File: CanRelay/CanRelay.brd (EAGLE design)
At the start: 93 x 65.5 mm, 24 parts

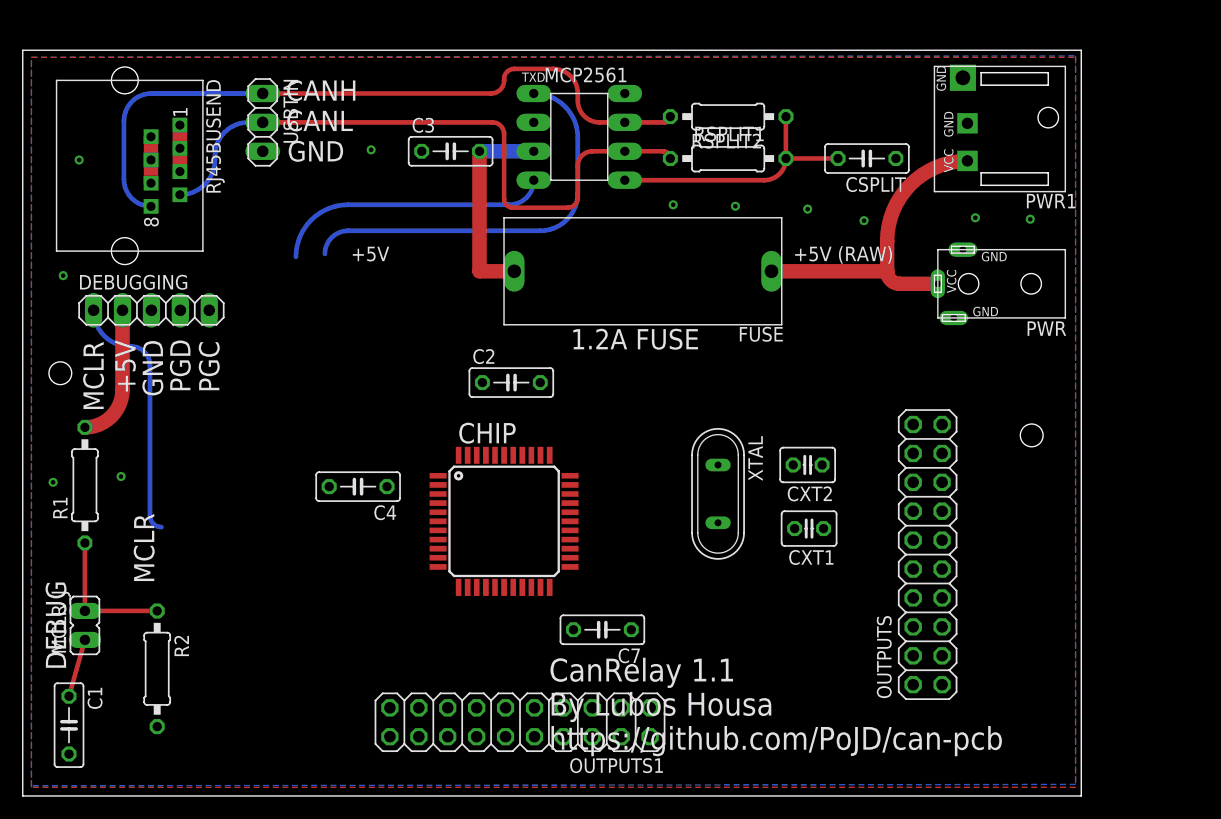
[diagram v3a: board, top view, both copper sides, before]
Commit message: #19 connected all but output ports, including RXD and TXD on both schema and the board, with no erc errors. Rotated the chip in the end to get MCLR and programming up and RX and TX closer to the transceiver. all seems sort of OKish so far, missing all outputs which are likely to mess things up
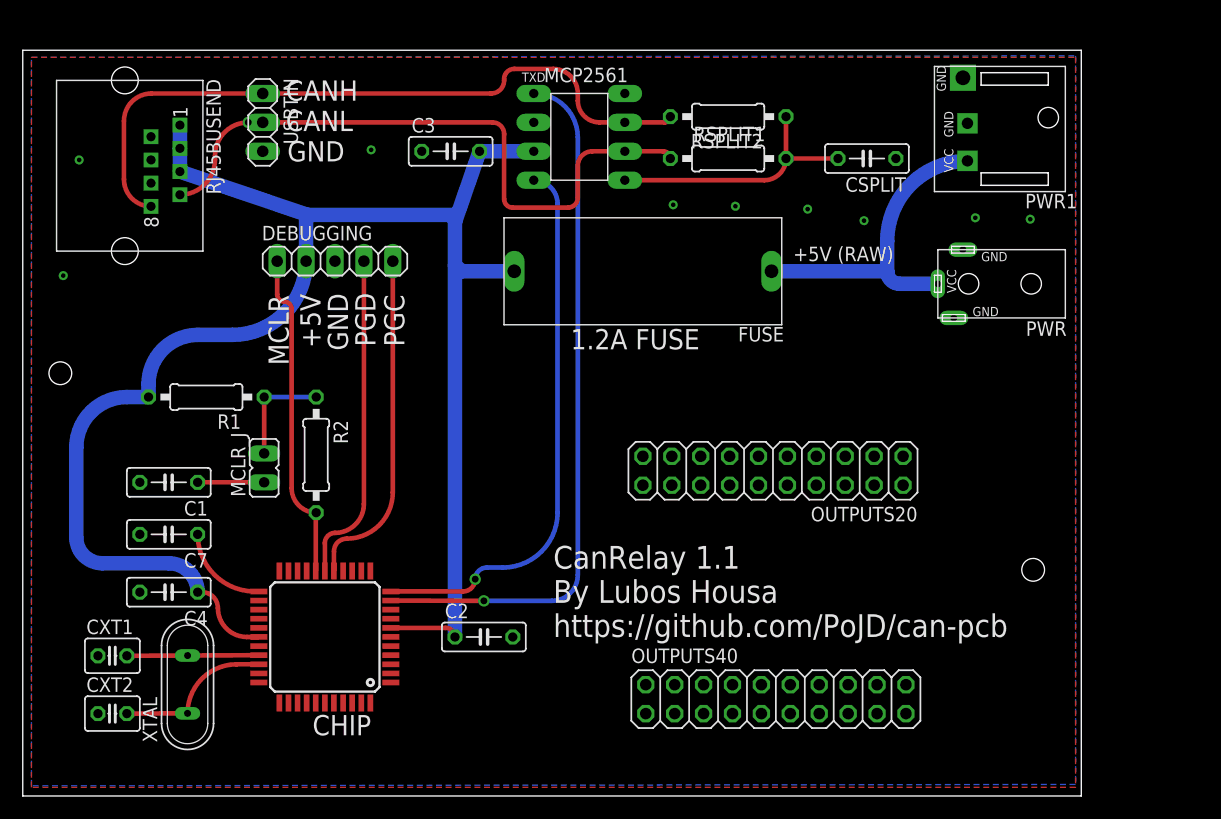
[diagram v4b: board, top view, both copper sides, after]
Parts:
- removed OUTPUTS, OUTPUTS1: (no value), pinhead:2X10
- added OUTPUTS20, OUTPUTS40: (no value), pinhead:2X10
- moved CXT2 64.9 mm to (7.87, 7.24), turned to 0 degrees
- moved CXT1 62.2 mm to (7.87, 12.3), turned to 0 degrees
- moved XTAL 49.5 mm to (14.5, 9.80), turned to 90 degrees
- moved C7 39.0 mm to (12.8, 23.0)
- moved R2 23.4 mm to (25.8, 30.0)
- moved C1 23.1 mm to (12.8, 27.6), turned to 180 degrees
- moved C2 22.5 mm to (40.5, 14.0)
- moved MCLR_J 21.0 mm to (21.2, 28.8)
- moved C4 19.0 mm to (12.8, 17.9)
- moved CHIP 18.7 mm to (26.5, 14.0), turned to 180 degrees
- moved DEBUGGING 16.7 mm to (27.4, 47.0)
- moved R1 13.2 mm to (16.1, 35.1), turned to 180 degrees
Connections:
- removed net N$4: C7.2, CHIP.23
- removed net PGC/O15: DEBUGGING.5, OUTPUTS.18
- removed net PGD/O16: DEBUGGING.4, OUTPUTS.20
- new net ENVREG: C7.1, CHIP.23
- new net O15: OUTPUTS20.18
- new net O16: OUTPUTS20.20
- new net PGC: CHIP.16, DEBUGGING.5
- new net PGD: CHIP.17, DEBUGGING.4
- net GND: now also C7.2; no longer C7.1
- net O1: now also OUTPUTS20.17; no longer OUTPUTS.17
- net O10: now also OUTPUTS20.12; no longer OUTPUTS.12
- net O13: now also OUTPUTS20.14; no longer OUTPUTS.14
- net O14: now also OUTPUTS20.16; no longer OUTPUTS.16
- net O17: now also OUTPUTS20.7; no longer OUTPUTS.7
- net O18: now also OUTPUTS20.5; no longer OUTPUTS.5
- net O19: now also OUTPUTS20.3; no longer OUTPUTS.3
- net O2: now also OUTPUTS20.15; no longer OUTPUTS.15
- net O20: now also OUTPUTS20.1; no longer OUTPUTS.1
- net O21: now also OUTPUTS20.2; no longer OUTPUTS.2
- net O22: now also OUTPUTS20.4; no longer OUTPUTS.4
- net O23: now also OUTPUTS20.6; no longer OUTPUTS.6
- net O24: now also OUTPUTS20.8; no longer OUTPUTS.8
- net O3: now also OUTPUTS20.13; no longer OUTPUTS.13
- net O4: now also OUTPUTS20.11; no longer OUTPUTS.11
- net O6: now also OUTPUTS20.9; no longer OUTPUTS.9
- net O9: now also OUTPUTS20.10; no longer OUTPUTS.10
- net RXD: now also CHIP.11
- net TXD: now also CHIP.10
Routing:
- net +5V: track 35.0 -> 148.0 mm
- net PGC: track 0.00 -> 29.4 mm
- net PGD: track 0.00 -> 28.6 mm
- net TXD: track 34.8 -> 61.3 mm, vias 0 -> 1
- net RXD: track 23.7 -> 47.6 mm, vias 0 -> 1
- net OSC2: track 0.00 -> 13.4 mm
- net OSC1: track 0.00 -> 11.6 mm
- net ENVREG: track 0.00 -> 7.45 mm
- net MCLR: track 21.6 -> 28.7 mm
- net GND: track 4.08 -> 0.00 mm, vias 11 -> 9
- net N$2: track 12.3 -> 9.52 mm
- net N$1: track 5.15 -> 5.84 mm
- net CANL: vias 0 -> 1
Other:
- board text removed: "DEBUG"
- board text removed: "RXD"
- board text removed: "TXD"

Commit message: #19 started connecting output ports. Bottom pat all done, also labeled properly, moved the whole PCB a few mms up to make space for routes there
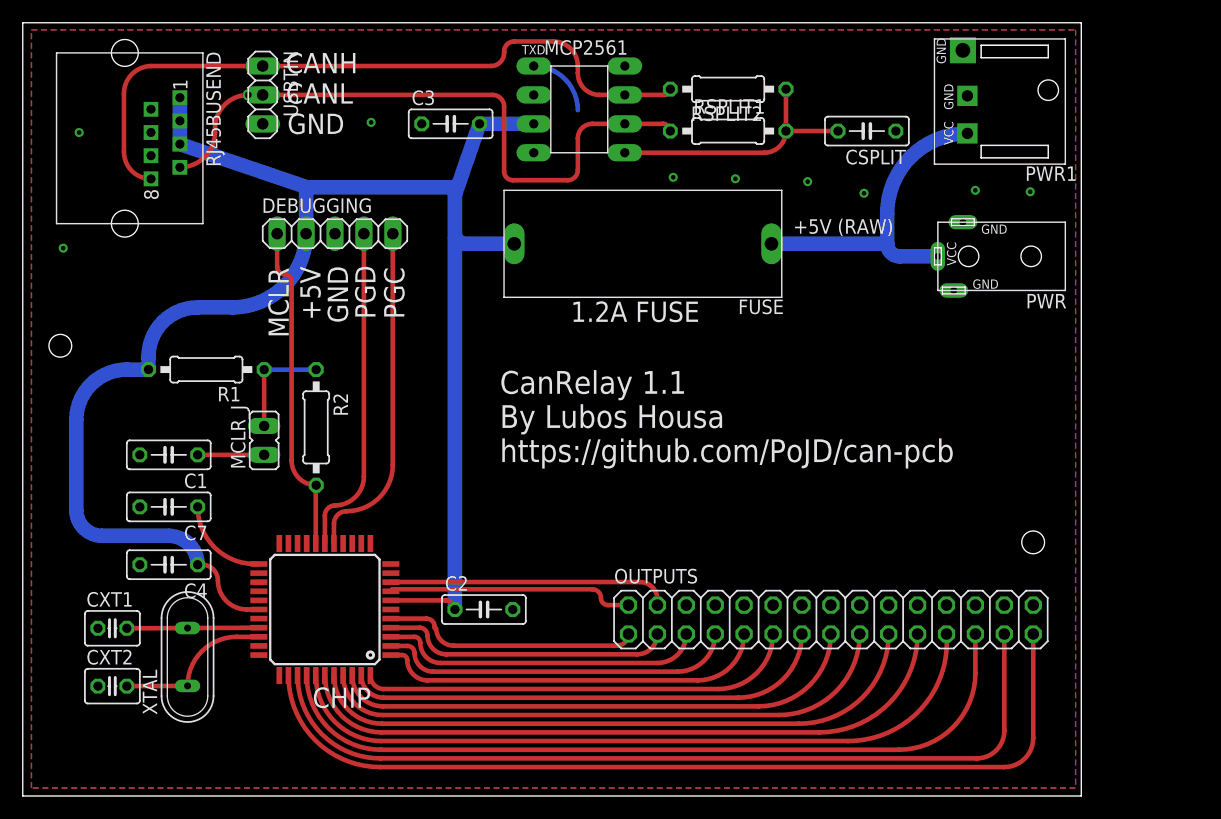
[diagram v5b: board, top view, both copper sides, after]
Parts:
- removed OUTPUTS20, OUTPUTS40: (no value), pinhead:2X10
- added OUTPUTS: (no value), pinhead:2X15
- moved CSPLIT 2.41 mm to (74.2, 58.4)
- moved FUSE 2.41 mm to (54.5, 48.5)
- moved MCP2561 2.41 mm to (48.9, 60.3)
- moved R1 2.41 mm to (16.1, 37.5)
- moved RSPLIT1 2.41 mm to (62.0, 58.4)
- moved RSPLIT2 2.41 mm to (62.0, 62.1)
- moved C1 2.41 mm to (12.8, 30.0)
- moved C4 2.41 mm to (12.8, 20.3)
- moved C7 2.41 mm to (12.8, 25.4)
- moved MCLR_J 2.41 mm to (21.2, 31.2)
- moved CXT2 2.41 mm to (7.87, 9.65)
- moved C2 2.41 mm to (40.5, 16.4)
- moved CHIP 2.41 mm to (26.5, 16.4)
- moved CXT1 2.41 mm to (7.87, 14.7)
- moved XTAL 2.41 mm to (14.5, 12.2)
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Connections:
- new net N$10: CHIP.14
- new net N$11: CHIP.15
- new net N$12: CHIP.19
- new net N$13: CHIP.20
- new net N$14: CHIP.21
- new net N$15: CHIP.22
- new net N$25: CHIP.27
- new net N$26: CHIP.26
- new net N$27: CHIP.25
- new net N$28: CHIP.24
- new net O11: CHIP.44, OUTPUTS.11
- new net O12: OUTPUTS.12
- new net O25: CHIP.37, OUTPUTS.25
- new net O26: OUTPUTS.26
- new net O27: CHIP.36, OUTPUTS.27
- new net O28: OUTPUTS.28
- new net O29: CHIP.35, OUTPUTS.29
- new net O30: CHIP.32, OUTPUTS.30
- new net O5: CHIP.3, OUTPUTS.5
- new net O7: CHIP.2, OUTPUTS.7
- new net O8: OUTPUTS.8
- net O1: now also CHIP.5, OUTPUTS.1; no longer OUTPUTS20.17
- net O10: now also OUTPUTS.10; no longer OUTPUTS20.12
- net O13: now also CHIP.43, OUTPUTS.13; no longer OUTPUTS20.14
- net O14: now also OUTPUTS.14; no longer OUTPUTS20.16
- net O15: now also CHIP.42, OUTPUTS.15; no longer OUTPUTS20.18
- net O16: now also OUTPUTS.16; no longer OUTPUTS20.20
- net O17: now also CHIP.41, OUTPUTS.17; no longer OUTPUTS20.7
- net O18: now also OUTPUTS.18; no longer OUTPUTS20.5
- net O19: now also CHIP.40, OUTPUTS.19; no longer OUTPUTS20.3
- net O2: now also CHIP.8, OUTPUTS.2; no longer OUTPUTS20.15
- net O20: now also OUTPUTS.20; no longer OUTPUTS20.1
- net O21: now also CHIP.39, OUTPUTS.21; no longer OUTPUTS20.2
- net O22: now also OUTPUTS.22; no longer OUTPUTS20.4
- net O23: now also CHIP.38, OUTPUTS.23; no longer OUTPUTS20.6
- net O24: now also OUTPUTS.24; no longer OUTPUTS20.8
- net O3: now also CHIP.4, OUTPUTS.3; no longer OUTPUTS20.13
- net O4: now also CHIP.9, OUTPUTS.4; no longer OUTPUTS20.11
- net O6: now also OUTPUTS.6; no longer OUTPUTS20.9
- net O9: now also CHIP.1, OUTPUTS.9; no longer OUTPUTS20.10
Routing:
- net O29: track 0.00 -> 79.0 mm
- net O27: track 0.00 -> 74.6 mm
- net O25: track 0.00 -> 67.7 mm
- net O23: track 0.00 -> 61.9 mm
- net O21: track 0.00 -> 57.7 mm
- net TXD: track 61.3 -> 5.48 mm, vias 1 -> 0
- net O19: track 0.00 -> 53.8 mm
- net O17: track 0.00 -> 49.8 mm
- net RXD: track 47.6 -> 0.00 mm, vias 1 -> 0
- net O15: track 0.00 -> 45.8 mm
- net O13: track 0.00 -> 41.8 mm
- net O11: track 0.00 -> 37.9 mm
- net O9: track 0.00 -> 33.6 mm
- net O7: track 0.00 -> 30.8 mm
- net O5: track 0.00 -> 28.0 mm
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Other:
- board size 93 x 65.5 mm -> 93 x 67.9 mm

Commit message: #19 wired all up. Rewired bottom part a bit too to avoid clearance errors, rather more space down there. Also rewired +5V a bit close to MCLR resistor. Also routed RXD and TXD and PGC and PGD and chose the most feasible outputs to wire them up to. Ran DRC and error checks, all fine now. Missing checking all, adding labels
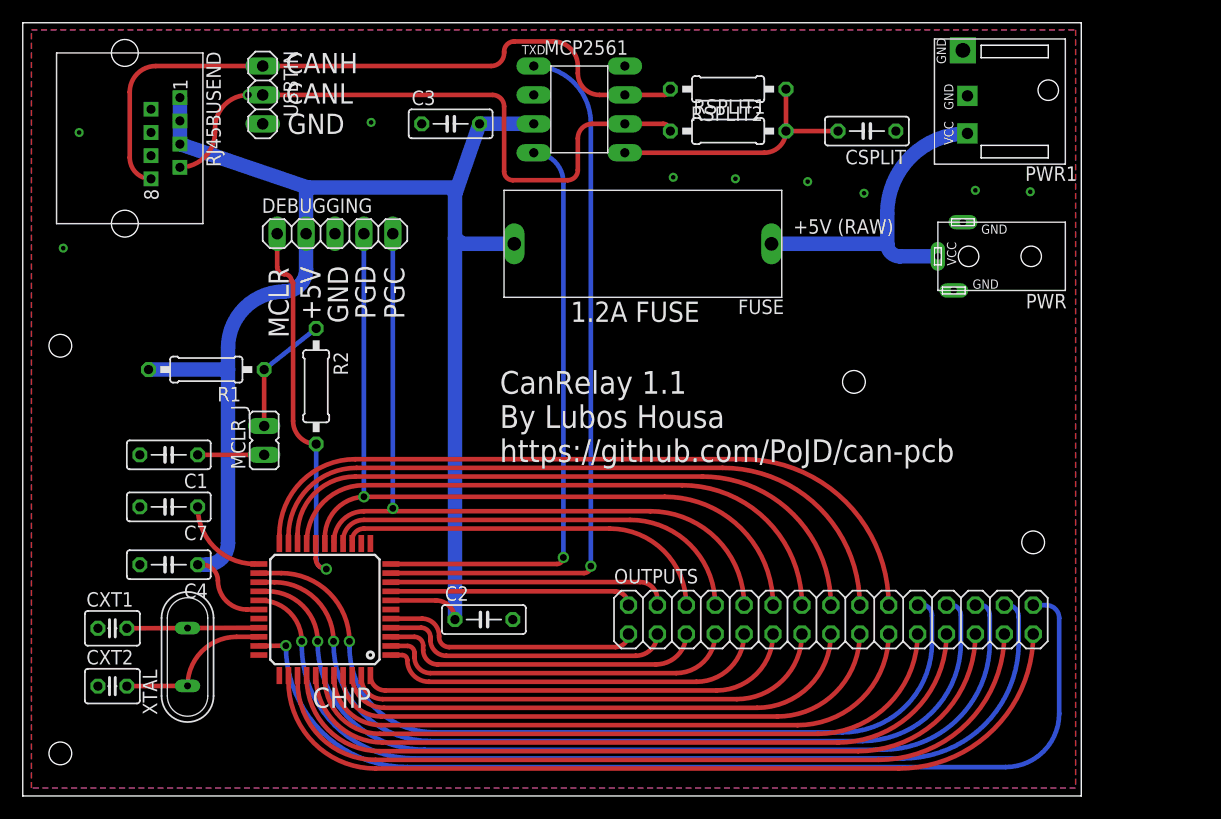
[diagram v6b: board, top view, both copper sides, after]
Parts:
- moved R2 3.62 mm to (25.8, 36.0)
- moved C2 0.88 mm to (40.5, 15.5)
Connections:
- removed net N$10: CHIP.14
- removed net N$11: CHIP.15
- removed net N$12: CHIP.19
- removed net N$13: CHIP.20
- removed net N$14: CHIP.21
- removed net N$15: CHIP.22
- removed net N$25: CHIP.27
- removed net N$26: CHIP.26
- removed net N$27: CHIP.25
- removed net N$28: CHIP.24
- removed net O10: OUTPUTS.10
- removed net O12: OUTPUTS.12
- removed net PGC: CHIP.16, DEBUGGING.5
- removed net PGD: CHIP.17, DEBUGGING.4
- new net O10/PGC: CHIP.16, DEBUGGING.5, OUTPUTS.10
- new net O12/PGD: CHIP.17, DEBUGGING.4, OUTPUTS.12
- net O14: now also CHIP.19
- net O16: now also CHIP.20
- net O18: now also CHIP.21
- net O20: now also CHIP.22
- net O22: now also CHIP.24
- net O24: now also CHIP.25
- net O26: now also CHIP.26
- net O28: now also CHIP.27
- net O6: now also CHIP.14
- net O8: now also CHIP.15
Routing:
- net O30: track 0.00 -> 87.8 mm, vias 0 -> 1
- net O28: track 0.00 -> 80.9 mm, vias 0 -> 1
- net O26: track 0.00 -> 77.9 mm, vias 0 -> 1
- net O24: track 0.00 -> 75.1 mm, vias 0 -> 1
- net O22: track 0.00 -> 72.5 mm, vias 0 -> 1
- net O12/PGD: track 0.00 -> 68.5 mm, vias 0 -> 1
- net O10/PGC: track 0.00 -> 65.1 mm, vias 0 -> 1
- net O20: track 0.00 -> 62.4 mm
- net TXD: track 5.48 -> 63.8 mm, vias 0 -> 1
- net O18: track 0.00 -> 58.3 mm
- net O16: track 0.00 -> 54.5 mm
- net RXD: track 0.00 -> 52.0 mm, vias 0 -> 1
- net O14: track 0.00 -> 50.1 mm
- net O8: track 0.00 -> 36.8 mm
- net O6: track 0.00 -> 32.9 mm
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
